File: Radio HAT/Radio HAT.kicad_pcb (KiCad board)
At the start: 4 copper layers, 65 x 45 mm, 29 parts, among them J1 Raspberry_Pi_2_3, J2 Coax SMA, J3 Barrel_Jack, J4 VCC, J5 6V, J6 GND, J7 V_RF, U1 RFM98PW, U2 AZ2185D-ADJTRG1

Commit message: Changes for v1.2
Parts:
- removed the G*** at (111.0, 123.0)
- added H3: M, MountingHole:MountingHole_2.7mm_M2.5_Pad_Via, F.Cu at (103.5, 152.5)
- added H4: M, MountingHole:MountingHole_2.7mm_M2.5_Pad_Via, F.Cu at (161.5, 152.5)
- added R10: 0, Resistor_SMD:R_0805_2012Metric_Pad1.20x1.40mm_HandSolder, F.Cu at (154.0, 110.0)
- added R11: 0, Resistor_SMD:R_0805_2012Metric_Pad1.20x1.40mm_HandSolder, F.Cu at (151.5, 110.0)
- added R12: 0, Resistor_SMD:R_0805_2012Metric_Pad1.20x1.40mm_HandSolder, F.Cu at (149.0, 110.0)
- added R13: 0, Resistor_SMD:R_0805_2012Metric_Pad1.20x1.40mm_HandSolder, F.Cu at (146.5, 110.0)
- added R14: 0, Resistor_SMD:R_0805_2012Metric_Pad1.20x1.40mm_HandSolder, F.Cu at (144.0, 110.0)
- added R15: DNP, Resistor_SMD:R_0805_2012Metric_Pad1.20x1.40mm_HandSolder, F.Cu at (114.0, 117.5)
- added R9: 0, Resistor_SMD:R_0805_2012Metric_Pad1.20x1.40mm_HandSolder, F.Cu at (156.5, 110.0)
- moved R5 10.5 mm to (143.0, 152.5)
- moved R1 8.08 mm to (112.0, 123.5)
- moved C3 8.00 mm to (109.0, 142.5)
- moved C4 8.00 mm to (109.0, 148.5)
- moved D1 8.00 mm to (121.5, 140.5)
- moved R3 8.00 mm to (119.5, 148.5)
- moved R4 8.00 mm to (121.5, 145.5)
- moved R6 8.00 mm to (121.5, 143.0)
- moved R8 8.00 mm to (121.5, 138.0)
- moved RV1 8.00 mm to (135.5, 137.9)
- moved U2 8.00 mm to (114.3, 147.0)
- moved R2 7.76 mm to (115.5, 123.5)
- moved J7 7.50 mm to (162.5, 127.0)
- moved G*** 7.32 mm to (146.0, 137.2)
- moved C1 7.31 mm to (160.5, 122.8)
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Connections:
- C5 pad 1: +3V3 -> /RF_3V3
- C6 pad 1: +3V3 -> /RF_3V3
- U1 pad 15: /RF_DIO5 -> Net-(U1-GPIO_5)
- U1 pad 3: /RF_DIO3 -> Net-(U1-GPIO_3)
- U1 pad 4: /RF_DIO4 -> Net-(U1-GPIO_4)
- U1 pad 6: /RF_DIO0 -> Net-(U1-GPIO_0)
- U1 pad 7: /RF_DIO1 -> Net-(U1-GPIO_1)
- U1 pad 8: /RF_DIO2 -> Net-(U1-GPIO_2)
- U1 pad 9: +3V3 -> /RF_3V3
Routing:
- net Net-(U1-GPIO_5): track 0.00 -> 35.5 mm, vias 0 -> 2
- net /RF_DIO5: track 47.0 -> 12.4 mm, vias 1 -> 0
- net Net-(U1-GPIO_3): track 0.00 -> 20.5 mm
- net Net-(U1-GPIO_4): track 0.00 -> 19.6 mm, vias 0 -> 2
- net GND: track 21.9 -> 3.06 mm, vias 164 -> 33
- net Net-(U1-GPIO_0): track 0.00 -> 17.4 mm, vias 0 -> 2
- net /RF_DIO3: track 19.2 -> 4.23 mm, vias 1 -> 0
- net Net-(U1-GPIO_1): track 0.00 -> 10.0 mm, vias 0 -> 2
- net +6V: track 34.4 -> 24.7 mm
- net /V_RF: track 55.3 -> 45.8 mm
- net Net-(U1-GPIO_2): track 0.00 -> 9.21 mm
- net /RF_3V3: track 0.00 -> 7.51 mm
- net /RF_RESET: track 41.3 -> 48.7 mm
- net /RF_CS: track 30.2 -> 37.4 mm
- net /RF_DIO4: track 21.6 -> 15.3 mm
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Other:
- board size 65 x 45 mm -> 65 x 56 mm
- board text added: "D0"
- board text added: "D1"
- board text added: "D2"
- board text added: "D3"
- board text added: "D4"
- board text added: "D5"

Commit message: Changes for v1.2
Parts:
- added J8: GPIO, TerminalBlock_TE-Connectivity:TerminalBlock_TE_282834-4_1x04_P2.54mm_Horizontal, F.Cu at (144.8, 152.4)
- added Q1: NMOS, Package_TO_SOT_SMD:SOT-23-3, F.Cu at (125.0, 112.0)
- moved R5 10.0 mm to (133.0, 152.5)
- moved RV1 2.00 mm to (135.5, 135.9)
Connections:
- J1 pad 15: unconnected-(J1-GPIO22-Pad15) -> /RX_EN
- J1 pad 16: unconnected-(J1-GPIO23-Pad16) -> /TX_EN
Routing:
- net /RX_EN: track 0.00 -> 59.9 mm, vias 0 -> 1
- net Net-(J8-Pin_1): track 0.00 -> 49.5 mm
- net /V_RF: track 45.8 -> 27.1 mm
- net /TX_EN: track 0.00 -> 9.54 mm, vias 0 -> 1
- net /REG_POT: track 13.5 -> 15.4 mm
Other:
- board text added: "RX"
- board text added: "TX"

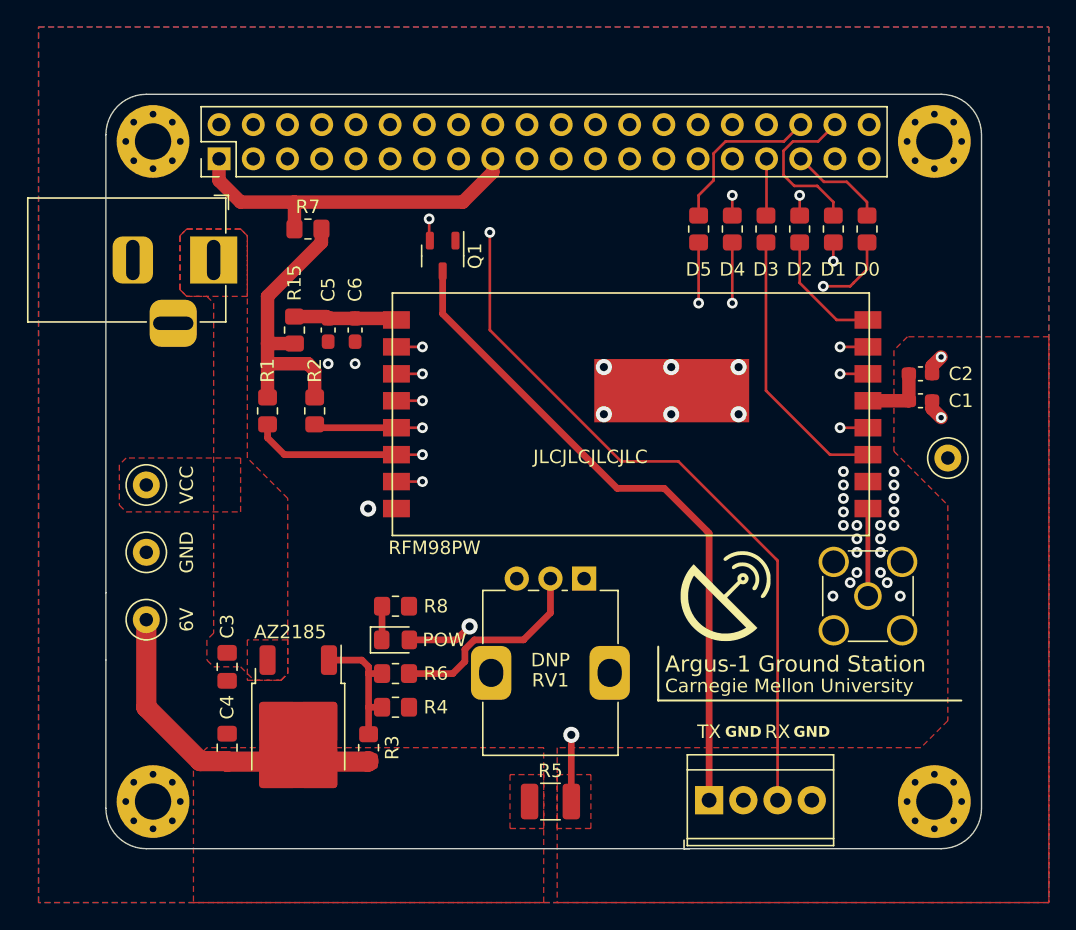
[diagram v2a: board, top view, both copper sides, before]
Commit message: Fixed TX and RX enable circuits
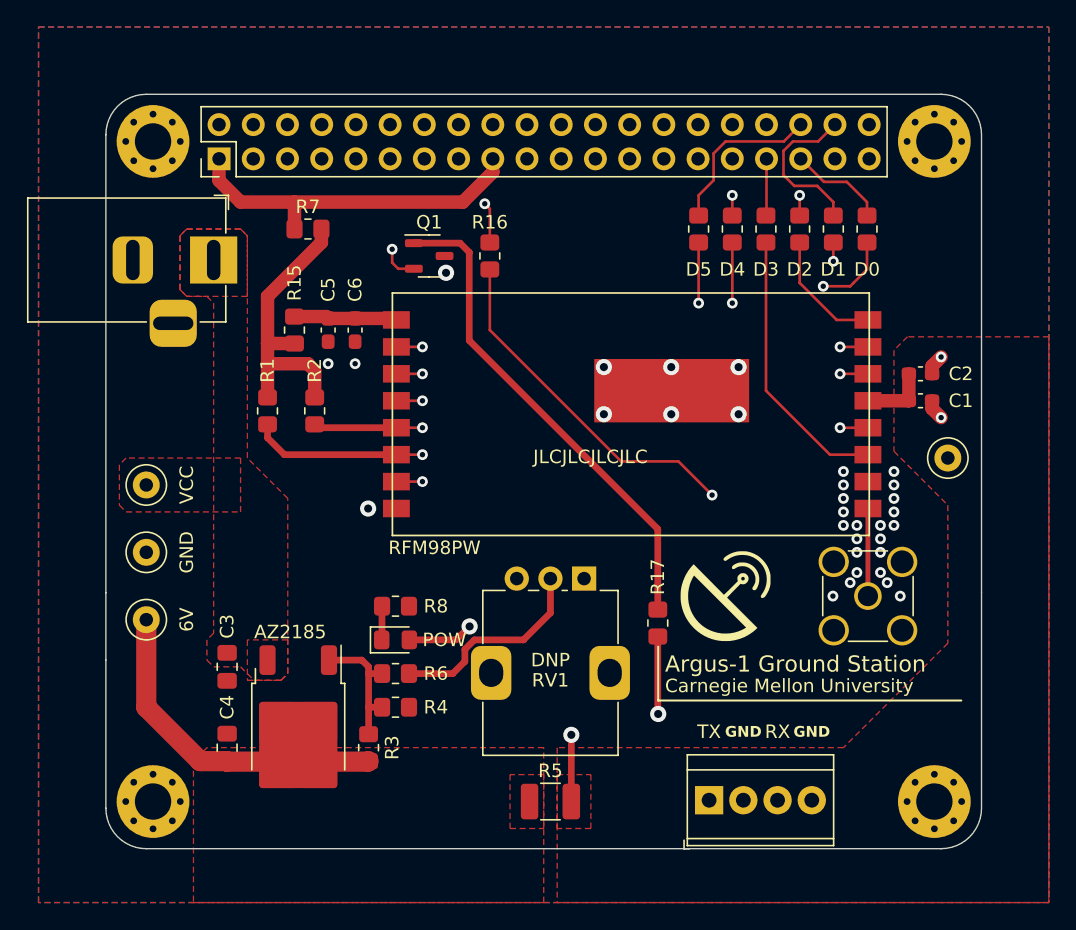
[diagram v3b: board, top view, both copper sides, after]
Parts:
- added R16: DNP, Resistor_SMD:R_0805_2012Metric_Pad1.20x1.40mm_HandSolder, F.Cu at (128.5, 112.0)
- added R17: DNP, Resistor_SMD:R_0805_2012Metric_Pad1.20x1.40mm_HandSolder, F.Cu at (141.0, 139.2)
- moved Q1 1.00 mm to (124.0, 112.0), turned to 0 degrees
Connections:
- J1 pad 15: /RX_EN -> /PI_RX_CTRL
- J1 pad 16: /TX_EN -> /PI_TX_CTRL
- J8 pad 1: Net-(J8-Pin_1) -> /TX_EN
- Q1 pad 1: +6V -> Net-(Q1-D)
- Q1 pad 2: /TX_EN -> /PI_TX_CTRL
- Q1 pad 3: Net-(J8-Pin_1) -> GND
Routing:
- net Net-(J8-Pin_1): track 49.5 -> 0.00 mm
- net Net-(Q1-D): track 0.00 -> 36.7 mm
- net /PI_TX_CTRL: track 0.00 -> 15.4 mm, vias 0 -> 1
- net /RX_EN: track 59.9 -> 50.7 mm
- net /PI_RX_CTRL: track 0.00 -> 7.17 mm, vias 0 -> 1
- net /TX_EN: track 9.54 -> 14.8 mm
- net GND: vias 33 -> 34

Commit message: Added stitching vias
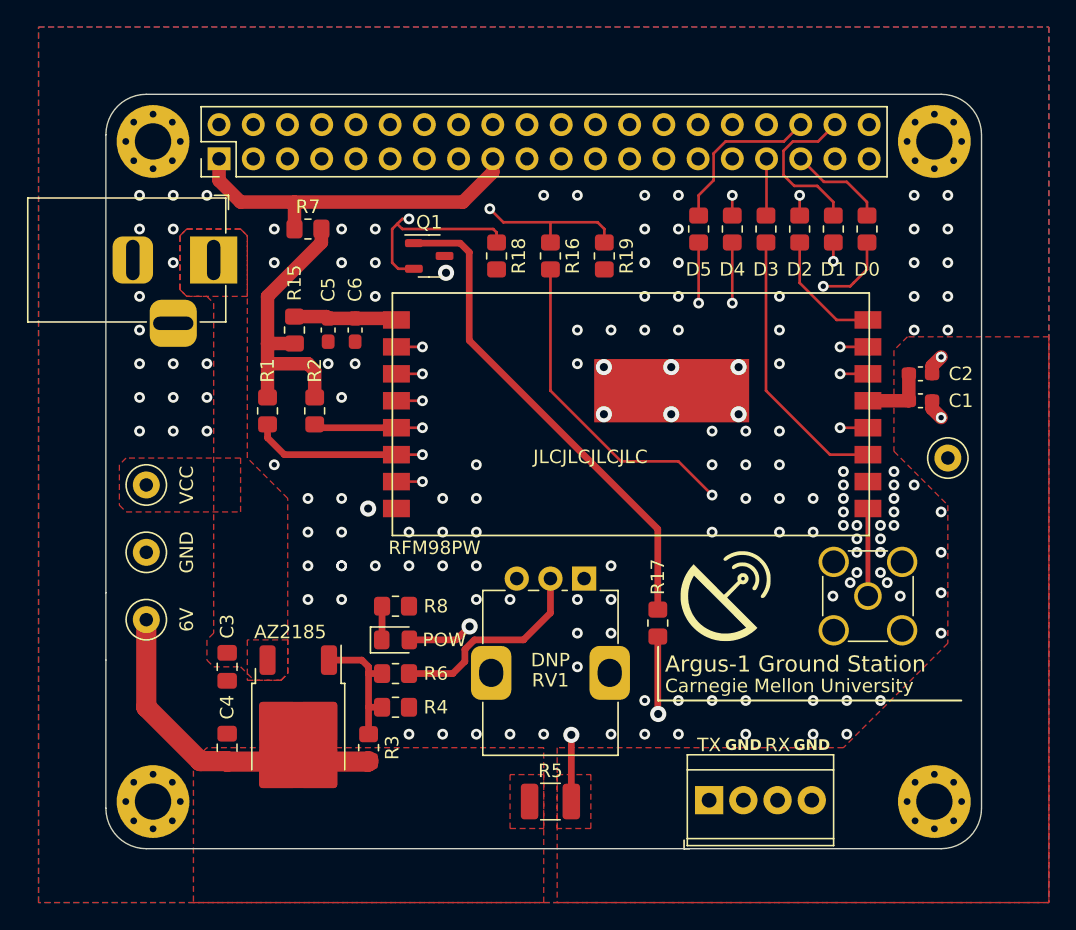
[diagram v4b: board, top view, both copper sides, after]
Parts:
- added R18: 1M, Resistor_SMD:R_0805_2012Metric_Pad1.20x1.40mm_HandSolder, F.Cu at (129.0, 112.0)
- added R19: 1M, Resistor_SMD:R_0805_2012Metric_Pad1.20x1.40mm_HandSolder, F.Cu at (137.0, 112.0)
- moved R16 4.50 mm to (133.0, 112.0)
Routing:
- net /PI_RX_CTRL: track 7.17 -> 16.3 mm
- net /PI_TX_CTRL: track 15.4 -> 23.8 mm
- net /RX_EN: track 50.7 -> 48.9 mm
- net GND: vias 34 -> 150

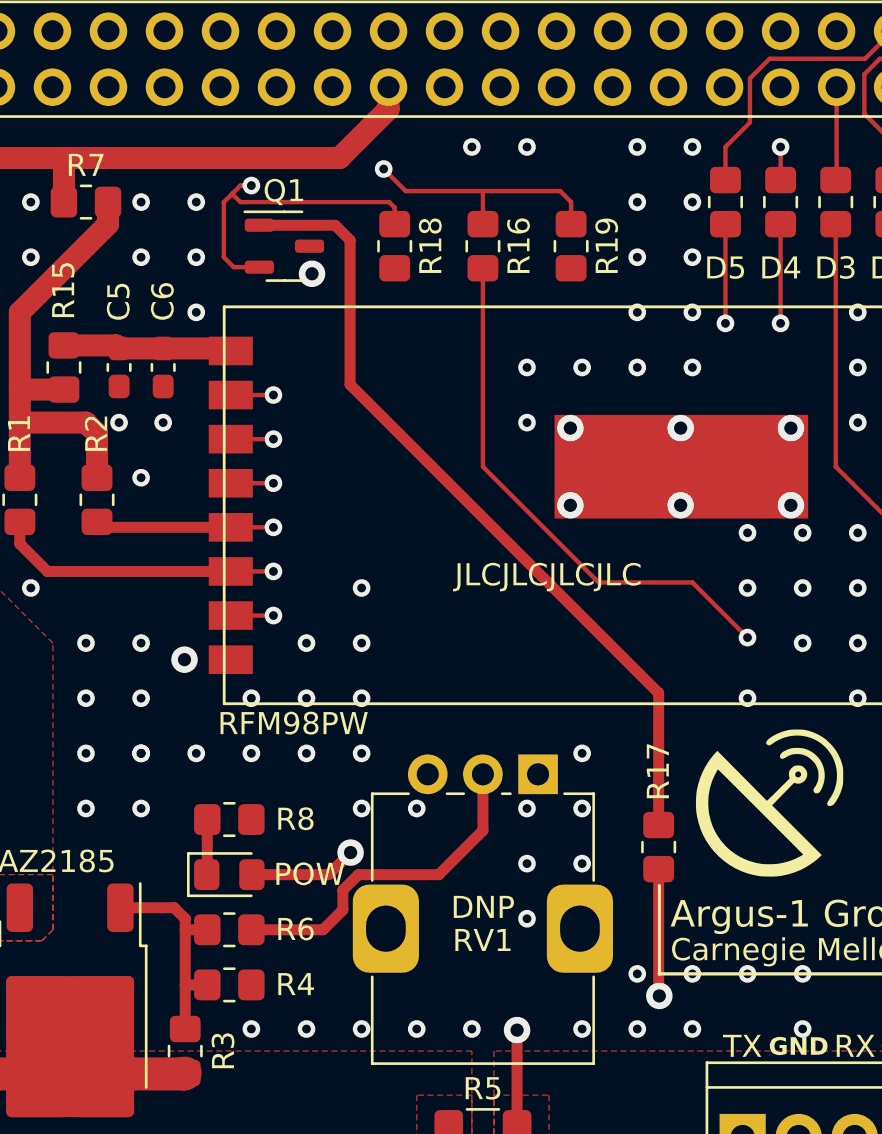
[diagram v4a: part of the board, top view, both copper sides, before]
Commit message: Add bypass resistor on TX GPIO control, ground Pot
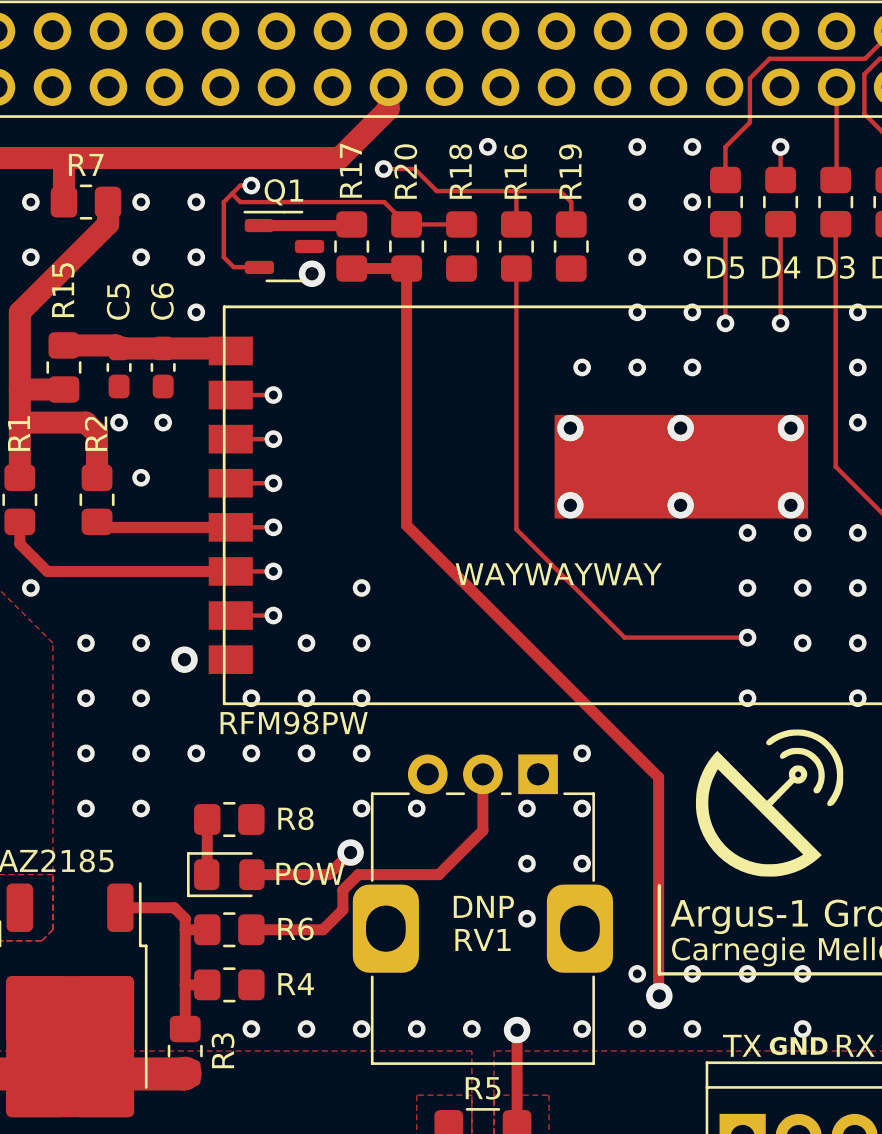
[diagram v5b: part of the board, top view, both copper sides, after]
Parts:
- added R20: DNP, Resistor_SMD:R_0805_2012Metric_Pad1.20x1.40mm_HandSolder, F.Cu at (129.5, 112.0)
- R16, R17: value DNP -> 0
- moved R17 30.6 mm to (127.1, 112.0)
- moved R18 3.03 mm to (132.0, 112.0)
- moved R16 1.52 mm to (134.5, 112.0)
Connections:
- RV1 pad MP: (no net) -> GND
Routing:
- net /TX_EN: track 14.8 -> 49.2 mm
- net Net-(Q1-D): track 36.7 -> 4.21 mm
- net /PI_TX_CTRL: track 23.8 -> 26.4 mm
- net GND: vias 150 -> 146
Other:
- board text added: "WAYWAYWAY"
- board text removed: "JLCJLCJLCJLC"

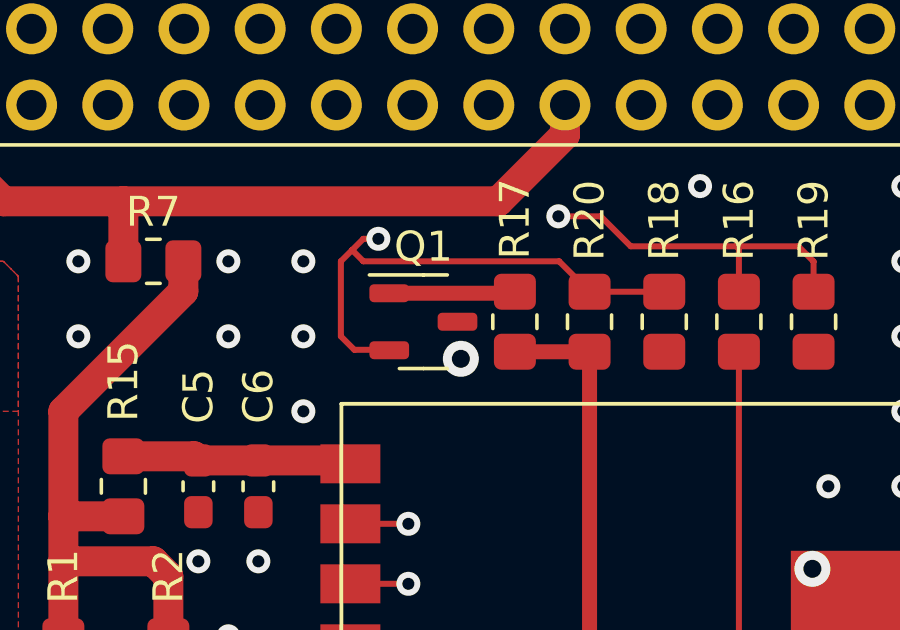
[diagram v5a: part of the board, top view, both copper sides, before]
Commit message: Fixed Q1 footprint
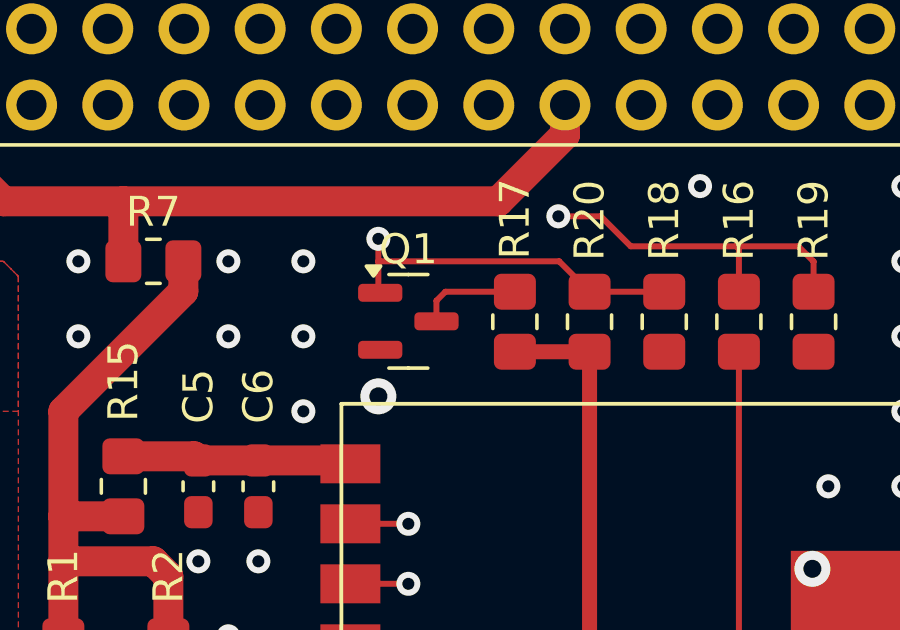
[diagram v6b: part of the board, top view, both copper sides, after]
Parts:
- Q1: value NMOS -> 2N7002; footprint Package_TO_SOT_SMD:SOT-23-3 -> Package_TO_SOT_SMD:SOT-23
- U2: value AZ2185D-ADJTRG1 -> AZ2185D-ADJTRG1
- moved Q1 0.50 mm to (123.5, 112.0)
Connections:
- Q1 pad 1: Net-(Q1-D) -> /PI_TX_CTRL
- Q1 pad 2: /PI_TX_CTRL -> GND
- Q1 pad 3: GND -> Net-(Q1-D)
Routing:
- net /PI_TX_CTRL: track 26.4 -> 21.3 mm
- net Net-(Q1-D): track 4.21 -> 3.50 mm
